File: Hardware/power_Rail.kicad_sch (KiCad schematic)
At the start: 2 parts

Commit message: fixed some subsheets
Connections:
- net +5V renamed 12VBuck/V_out_5V

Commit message: cleaned up schematic more
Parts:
- added D5: LED, LED_SMD:LED_0603_1608Metric, symbol lhrs_misc:Blue_LED
- added R28: 250, Package_TO_SOT_SMD:SOT-23, symbol Device:R
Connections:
- net GND: now also R28.2
- net Vout: now also D5.2 (A)
- new net: D5.1 (K), R28.1

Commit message: made review changes
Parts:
- added JP2, JP3, JP4, JP5: SolderJumper_2_Open, symbol Jumper:SolderJumper_2_Open
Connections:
- net 12VBuck/V_out_5V: now also JP3.2 (B)
- net GND: now also JP3.1 (A), JP4.1 (A)
- net MUX_OUT: now also JP5.1 (A)
- net Vin: now also JP2.1 (A)
- net Vout: now also JP5.2 (B)
- new net 12VBuck/V_in_12V: JP2.2 (B), JP4.2 (B)
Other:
- note added: "Galvanically Isolated"

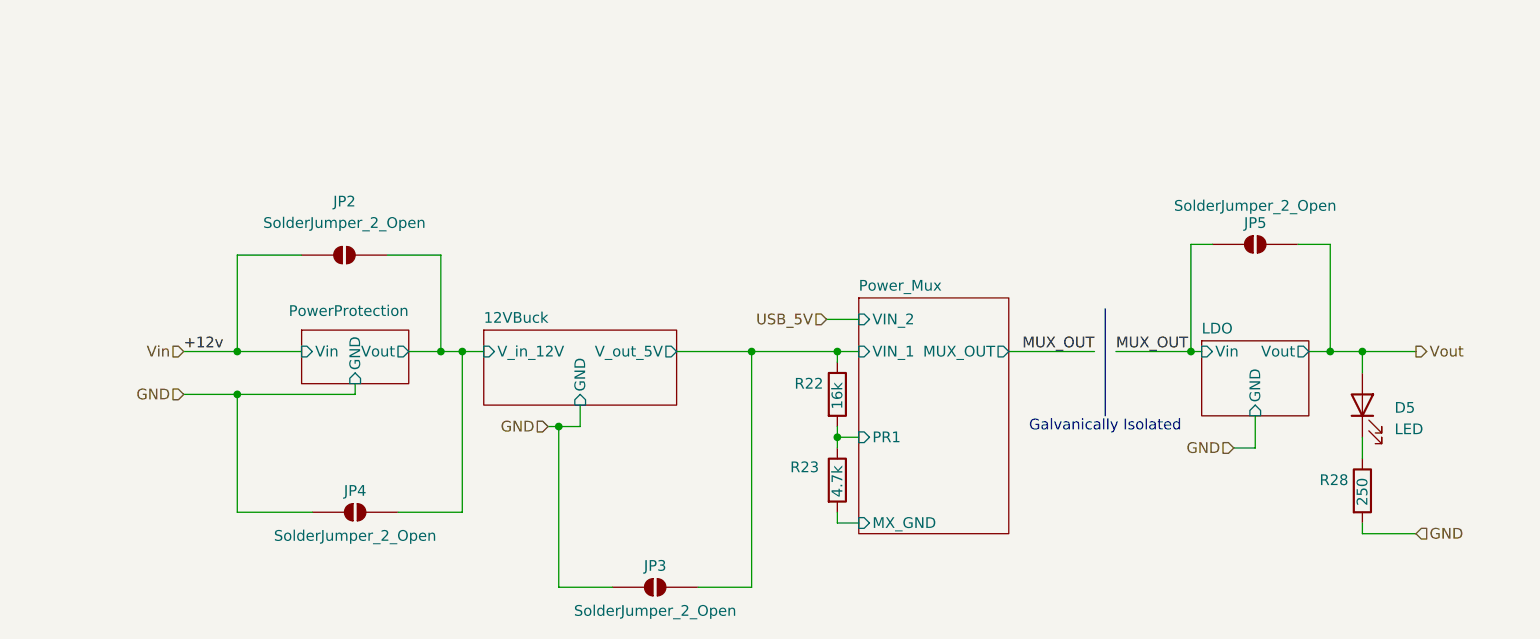
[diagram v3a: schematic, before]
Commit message: Added TestPoints
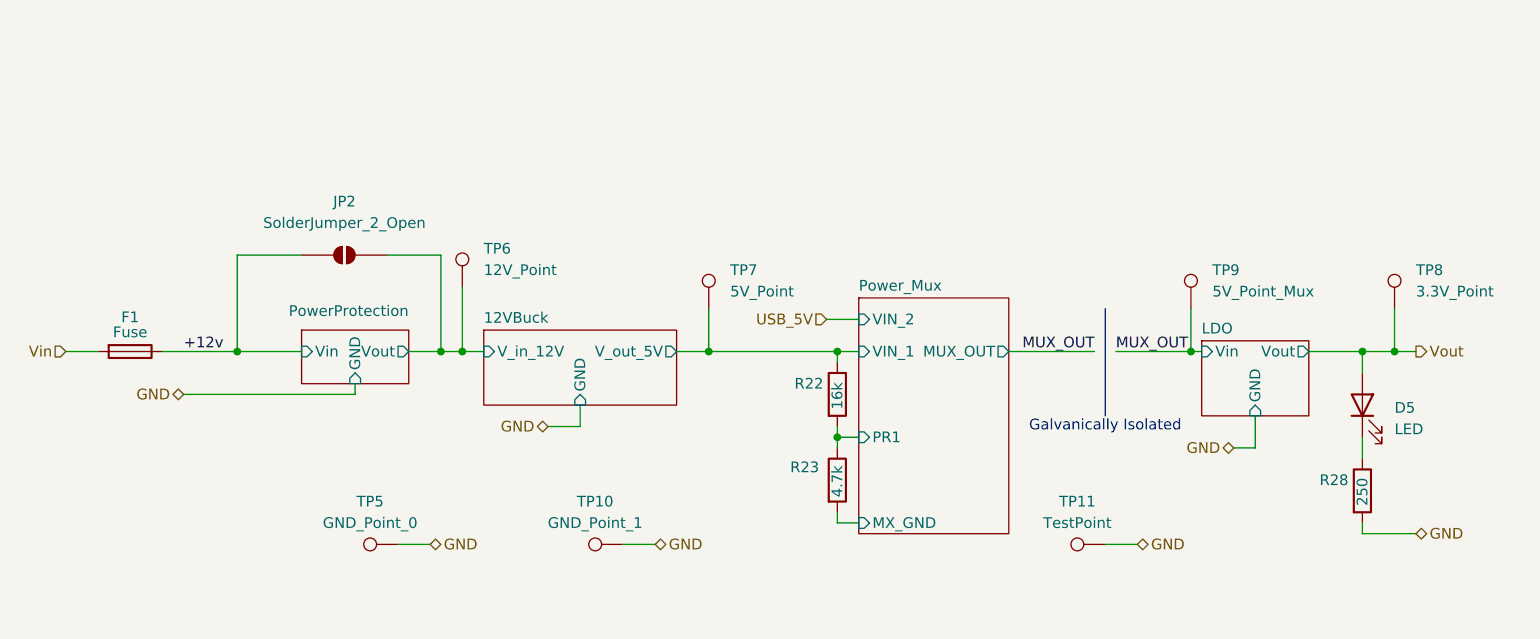
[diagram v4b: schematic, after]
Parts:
- removed JP3, JP4, JP5: SolderJumper_2_Open, symbol Jumper:SolderJumper_2_Open
- added F1: Fuse, symbol Device:Fuse
- added TP10: GND_Point_1, LHRS_Connectors:Molex_Nano-Fit_105310-xx10_2x05_P2.50mm_Vertical, symbol Connector:TestPoint
- added TP11: TestPoint, LHRS_Connectors:Molex_Nano-Fit_105310-xx10_2x05_P2.50mm_Vertical, symbol Connector:TestPoint
- added TP5: GND_Point_0, LHRS_Connectors:Molex_Nano-Fit_105310-xx10_2x05_P2.50mm_Vertical, symbol Connector:TestPoint
- added TP6: 12V_Point, LHRS_Connectors:Molex_Nano-Fit_105310-xx10_2x05_P2.50mm_Vertical, symbol Connector:TestPoint
- added TP7: 5V_Point, LHRS_Connectors:Molex_Nano-Fit_105310-xx10_2x05_P2.50mm_Vertical, symbol Connector:TestPoint
- added TP8: 3.3V_Point, LHRS_Connectors:Molex_Nano-Fit_105310-xx10_2x05_P2.50mm_Vertical, symbol Connector:TestPoint
- added TP9: 5V_Point_Mux, LHRS_Connectors:Molex_Nano-Fit_105310-xx10_2x05_P2.50mm_Vertical, symbol Connector:TestPoint
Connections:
- net 12VBuck/V_in_12V: now also TP6.1
- net 12VBuck/V_out_5V: now also TP7.1
- net GND: now also TP10.1, TP11.1, TP5.1
- net MUX_OUT: now also TP9.1
- net Vin: now also F1.2; no longer JP2.1 (A)
- net Vout: now also TP8.1
- new net +12v: F1.1, JP2.1 (A)

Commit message: Final Review Ready
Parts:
- removed D5: LED, LED_SMD:LED_0603_1608Metric, symbol lhrs_misc:Blue_LED
- removed R28: 250, Package_TO_SOT_SMD:SOT-23, symbol Device:R
- added D11, D12, D14: LED, LED_SMD:LED_0603_1608Metric_Pad1.05x0.95mm_HandSolder, symbol lhrs_misc:Blue_LED
- added R29: 1k, Package_TO_SOT_SMD:SOT-23, symbol Device:R
- added R30: 330, Package_TO_SOT_SMD:SOT-23, symbol Device:R
- added R31: 150, Package_TO_SOT_SMD:SOT-23, symbol Device:R
- added TP16: USB_5V_Point, LHRS_Connectors:Molex_Nano-Fit_105310-xx10_2x05_P2.50mm_Vertical, symbol Connector:TestPoint
- TP11: value TestPoint -> GND_Point_2
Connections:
- net +12v: now also R29.1
- net GND: now also D11.1 (K), D12.1 (K), D14.1 (K)
- net MUX_OUT: now also R30.1
- net USB_5V: now also TP16.1
- net Vout: now also R31.1
- new net: D11.2 (A), R29.2
- new net: D14.2 (A), R31.2
- new net: D12.2 (A), R30.2
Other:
- note added: "GND Test Points"
- moved on the sheet: TP10, TP11, TP5, TP6

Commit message: Final Changes before Final Review
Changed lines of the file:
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@@
 	(wire
 		(pts
-			(xy 95.25 87.63) (xy 99.06 87.63)
+			(xy 93.98 95.25) (xy 99.06 95.25)
 		)
 		(stroke
@@
 	(wire
 		(pts
-			(xy 99.06 85.09) (xy 99.06 87.63)
+			(xy 99.06 88.9) (xy 99.06 95.25)
 		)
 		(stroke
@@
 	(hierarchical_label "GND"
 		(shape bidirectional)
-		(at 95.25 87.63 180)
+		(at 93.98 95.25 180)
 		(effects
 			(font
@@
 		)
 		(instances
+			(project "power_Rail"
+				(path "/aa7870c6-fc66-461c-9d29-908d06b1b5db"
+					(reference "D11")
+					(unit 1)
+				)
+			)
 			(project "SuspensionBoard"
 				(path "/f9dc491a-b8c6-4623-9728-13837ac4bba3/bb9a0353-c4c7-4944-b892-c85c279a5c68"
@@
 		)
 		(instances
+			(project "power_Rail"
+				(path "/aa7870c6-fc66-461c-9d29-908d06b1b5db"
+					(reference "D14")
+					(unit 1)
+				)
+			)
 			(project "SuspensionBoard"
 				(path "/f9dc491a-b8c6-4623-9728-13837ac4bba3/bb9a0353-c4c7-4944-b892-c85c279a5c68"
@@
 		)
 		(instances
+			(project "power_Rail"
+				(path "/aa7870c6-fc66-461c-9d29-908d06b1b5db"
+					(reference "TP11")
+					(unit 1)
+				)
+			)
 			(project "SuspensionBoard"
 				(path "/f9dc491a-b8c6-4623-9728-13837ac4bba3/bb9a0353-c4c7-4944-b892-c85c279a5c68"
@@
 		)
 		(instances
+			(project "power_Rail"
+				(path "/aa7870c6-fc66-461c-9d29-908d06b1b5db"
+					(reference "TP5")
+					(unit 1)
+				)
+			)
 			(project "SuspensionBoard"
 				(path "/f9dc491a-b8c6-4623-9728-13837ac4bba3/bb9a0353-c4c7-4944-b892-c85c279a5c68"
@@
 		)
 		(instances
+			(project "power_Rail"
+				(path "/aa7870c6-fc66-461c-9d29-908d06b1b5db"
+					(reference "TP7")
+					(unit 1)
+				)
+			)
 			(project "SuspensionBoard"
 				(path "/f9dc491a-b8c6-4623-9728-13837ac4bba3/bb9a0353-c4c7-4944-b892-c85c279a5c68"
@@
 		)
 		(instances
+			(project "power_Rail"
+				(path "/aa7870c6-fc66-461c-9d29-908d06b1b5db"
+					(reference "R29")
+					(unit 1)
+				)
+			)
 			(project "SuspensionBoard"
 				(path "/f9dc491a-b8c6-4623-9728-13837ac4bba3/bb9a0353-c4c7-4944-b892-c85c279a5c68"
@@
 		)
 		(instances
+			(project "power_Rail"
+				(path "/aa7870c6-fc66-461c-9d29-908d06b1b5db"
+					(reference "R31")
+					(unit 1)
+				)
+			)
 			(project "SuspensionBoard"
 				(path "/f9dc491a-b8c6-4623-9728-13837ac4bba3/bb9a0353-c4c7-4944-b892-c85c279a5c68"
@@
 		)
 		(instances
+			(project "power_Rail"
+				(path "/aa7870c6-fc66-461c-9d29-908d06b1b5db"
+					(reference "TP6")
+					(unit 1)
+				)
+			)
 			(project "SuspensionBoard"
 				(path "/f9dc491a-b8c6-4623-9728-13837ac4bba3/bb9a0353-c4c7-4944-b892-c85c279a5c68"
@@
 		)
 		(instances
+			(project "power_Rail"
+				(path "/aa7870c6-fc66-461c-9d29-908d06b1b5db"
+					(reference "TP16")
+					(unit 1)
+				)
+			)
 			(project "SuspensionBoard"
 				(path "/f9dc491a-b8c6-4623-9728-13837ac4bba3/bb9a0353-c4c7-4944-b892-c85c279a5c68"
@@
 		)
 		(instances
+			(project "power_Rail"
+				(path "/aa7870c6-fc66-461c-9d29-908d06b1b5db"
+					(reference "TP8")
+					(unit 1)
+				)
+			)
 			(project "SuspensionBoard"
 				(path "/f9dc491a-b8c6-4623-9728-13837ac4bba3/bb9a0353-c4c7-4944-b892-c85c279a5c68"
@@
 		)
 		(instances
+			(project "power_Rail"
+				(path "/aa7870c6-fc66-461c-9d29-908d06b1b5db"
+					(reference "F1")
+					(unit 1)
+				)
+			)
 			(project "SuspensionBoard"
 				(path "/f9dc491a-b8c6-4623-9728-13837ac4bba3/bb9a0353-c4c7-4944-b892-c85c279a5c68"
@@
 		)
 		(instances
+			(project "power_Rail"
+				(path "/aa7870c6-fc66-461c-9d29-908d06b1b5db"
+					(reference "D12")
+					(unit 1)
+				)
+			)
 			(project "SuspensionBoard"
 				(path "/f9dc491a-b8c6-4623-9728-13837ac4bba3/bb9a0353-c4c7-4944-b892-c85c279a5c68"
@@
 		)
 		(instances
+			(project "power_Rail"
+				(path "/aa7870c6-fc66-461c-9d29-908d06b1b5db"
+					(reference "R30")
+					(unit 1)
+				)
+			)
 			(project "SuspensionBoard"
 				(path "/f9dc491a-b8c6-4623-9728-13837ac4bba3/bb9a0353-c4c7-4944-b892-c85c279a5c68"
@@
 		)
 		(instances
+			(project "power_Rail"
+				(path "/aa7870c6-fc66-461c-9d29-908d06b1b5db"
+					(reference "R23")
+					(unit 1)
+				)
+			)
 			(project "SuspensionBoard"
 				(path "/f9dc491a-b8c6-4623-9728-13837ac4bba3/bb9a0353-c4c7-4944-b892-c85c279a5c68"
@@
 		)
 		(instances
+			(project "power_Rail"
+				(path "/aa7870c6-fc66-461c-9d29-908d06b1b5db"
+					(reference "R22")
+					(unit 1)
+				)
+			)
 			(project "SuspensionBoard"
 				(path "/f9dc491a-b8c6-4623-9728-13837ac4bba3/bb9a0353-c4c7-4944-b892-c85c279a5c68"
@@
 		)
 		(instances
+			(project "power_Rail"
+				(path "/aa7870c6-fc66-461c-9d29-908d06b1b5db"
+					(reference "TP9")
+					(unit 1)
+				)
+			)
 			(project "SuspensionBoard"
 				(path "/f9dc491a-b8c6-4623-9728-13837ac4bba3/bb9a0353-c4c7-4944-b892-c85c279a5c68"
@@
 		)
 		(instances
+			(project "power_Rail"
+				(path "/aa7870c6-fc66-461c-9d29-908d06b1b5db"
+					(reference "JP2")
+					(unit 1)
+				)
+			)
 			(project "SuspensionBoard"
 				(path "/f9dc491a-b8c6-4623-9728-13837ac4bba3/bb9a0353-c4c7-4944-b892-c85c279a5c68"
@@
 		)
 		(instances
+			(project "power_Rail"
+				(path "/aa7870c6-fc66-461c-9d29-908d06b1b5db"
+					(reference "TP10")
+					(unit 1)
+				)
+			)
 			(project "SuspensionBoard"
 				(path "/f9dc491a-b8c6-4623-9728-13837ac4bba3/bb9a0353-c4c7-4944-b892-c85c279a5c68"
@@
 				)
 			)
+			(project "power_Rail"
+				(path "/aa7870c6-fc66-461c-9d29-908d06b1b5db"
+					(page "4")
+				)
+			)
 		)
 	)
@@
 				)
 			)
+			(project "power_Rail"
+				(path "/aa7870c6-fc66-461c-9d29-908d06b1b5db"
+					(page "3")
+				)
+			)
 		)
 	)
@@
 				)
 			)
+			(project "power_Rail"
+				(path "/aa7870c6-fc66-461c-9d29-908d06b1b5db"
+					(page "5")
+				)
+			)
 		)
 	)
 	(sheet
 		(at 92.71 78.74)
-		(size 12.7 6.35)
+		(size 12.7 10.16)
 		(exclude_from_sim no)
 		(in_bom yes)
@@
 		)
 		(pin "GND" input
-			(at 99.06 85.09 270)
+			(at 99.06 88.9 270)
 			(effects
 				(font
@@
 				)
 			)
-		)
-	)
+			(project "power_Rail"
+				(path "/aa7870c6-fc66-461c-9d29-908d06b1b5db"
+					(page "2")
+				)
+			)
+		)
+	)
+	(sheet_instances
+		(path "/"
+			(page "1")
+		)
+	)

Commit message: Updated KiCAD Sharepoint
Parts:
- removed TP6: 12V_Point, LHRS_Connectors:Molex_Nano-Fit_105310-xx10_2x05_P2.50mm_Vertical, symbol Connector:TestPoint
- JP2: value SolderJumper_2_Open -> PP_Bypass
- R29: value 1k -> 5k
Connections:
- net MUX_OUT renamed LDO/Vin
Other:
- note removed: "Galvanically Isolated"
- moved on the sheet: D14, R31, TP8, TP9

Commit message: Made some changes
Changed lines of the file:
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@@
+	)
+	(sheet
+		(at 198.12 77.47)
+		(size 12.7 11.43)
+		(exclude_from_sim no)
+		(in_bom yes)
+		(on_board yes)
+		(dnp no)
+		(fields_autoplaced yes)
+		(stroke
+			(width 0.1524)
+			(type solid)
+		)
+		(fill
+			(color 0 0 0 0)
+		)
+		(property "Sheetname" "LDO"
+			(at 198.12 76.7584 0)
+			(show_name no)
+			(do_not_autoplace no)
+			(effects
+				(font
+					(size 1.27 1.27)
+				)
+				(justify left bottom)
+			)
+		)
+		(property "Sheetfile" "LDO.kicad_sch"
+			(at 198.12 89.4846 0)
+			(hide yes)
+			(show_name no)
+			(do_not_autoplace no)
+			(effects
+				(font
+					(size 1.27 1.27)
+				)
+				(justify left top)
+			)
+		)
+		(pin "GND" input
+			(at 204.47 88.9 270)
+			(effects
+				(font
+					(size 1.27 1.27)
+				)
+				(justify left)
+			)
+		)
+		(pin "Vin" input
+			(at 198.12 81.28 180)
+			(effects
+				(font
+					(size 1.27 1.27)
+				)
+				(justify left)
+			)
+		)
+		(pin "Vout" output
+			(at 210.82 81.28 0)
+			(effects
+				(font
+					(size 1.27 1.27)
+				)
+				(justify right)
+			)
+		)
+		(instances
+			(project "SuspensionBoard"
+				(path "/f9dc491a-b8c6-4623-9728-13837ac4bba3/bb9a0353-c4c7-4944-b892-c85c279a5c68"
+					(page "4")
+				)
+			)
+		)
+	)
+	(sheet
+		(at 92.71 76.2)
+		(size 12.7 12.7)
+		(exclude_from_sim no)
+		(in_bom yes)
+		(on_board yes)
+		(dnp no)
+		(fields_autoplaced yes)
+		(stroke
+			(width 0.1524)
+			(type solid)
+		)
+		(fill
+			(color 0 0 0 0)
+		)
+		(property "Sheetname" "PowerProtection"
+			(at 92.71 75.4884 0)
+			(show_name no)
+			(do_not_autoplace no)
+			(effects
+				(font
+					(size 1.27 1.27)
+				)
+				(justify left bottom)
+			)
+		)
+		(property "Sheetfile" "PowerProtection.kicad_sch"
+			(at 92.71 89.4846 0)
+			(hide yes)
+			(show_name no)
+			(do_not_autoplace no)
+			(effects
+				(font
+					(size 1.27 1.27)
+				)
+				(justify left top)
+			)
+		)
+		(pin "GND" input
+			(at 99.06 88.9 270)
+			(effects
+				(font
+					(size 1.27 1.27)
+				)
+				(justify left)
+			)
+		)
+		(pin "Vin" input
+			(at 92.71 81.28 180)
+			(effects
+				(font
+					(size 1.27 1.27)
+				)
+				(justify left)
+			)
+		)
+		(pin "Vout" output
+			(at 105.41 81.28 0)
+			(effects
+				(font
+					(size 1.27 1.27)
+				)
+				(justify right)
+			)
+		)
+		(instances
+			(project "SuspensionBoard"
+				(path "/f9dc491a-b8c6-4623-9728-13837ac4bba3/bb9a0353-c4c7-4944-b892-c85c279a5c68"
+					(page "7")
+				)
+			)
+		)
+	)
+	(sheet
+		(at 114.3 77.47)
+		(size 22.86 10.16)
+		(exclude_from_sim no)
+		(in_bom yes)
+		(on_board yes)
+		(dnp no)
+		(fields_autoplaced yes)
+		(stroke
+			(width 0.1524)
+			(type solid)
+		)
+		(fill
+			(color 0 0 0 0)
+		)
+		(property "Sheetname" "12VBuck"
+			(at 114.3 76.7584 0)
+			(show_name no)
+			(do_not_autoplace no)
+			(effects
+				(font
+					(size 1.27 1.27)
+				)
+				(justify left bottom)
+			)
+		)
+		(property "Sheetfile" "12VBuck.kicad_sch"
+			(at 114.3 88.2146 0)
+			(hide yes)
+			(show_name no)
+			(do_not_autoplace no)
+			(effects
+				(font
+					(size 1.27 1.27)
+				)
+				(justify left top)
+			)
+		)
+		(pin "GND" input
+			(at 125.73 87.63 270)
+			(effects
+				(font
+					(size 1.27 1.27)
+				)
+				(justify left)
+			)
+		)
+		(pin "V_in_12V" input
+			(at 114.3 81.28 180)
+			(effects
+				(font
+					(size 1.27 1.27)
+				)
+				(justify left)
+			)
+		)
+		(pin "V_out_5V" output
+			(at 137.16 81.28 0)
+			(effects
+				(font
+					(size 1.27 1.27)
+				)
+				(justify right)
+			)
+		)
+		(instances
+			(project "SuspensionBoard"
+				(path "/f9dc491a-b8c6-4623-9728-13837ac4bba3/bb9a0353-c4c7-4944-b892-c85c279a5c68"
+					(page "3")
+				)
+			)
+		)
 	)
 	(sheet
@@
 				)
 			)
-			(project "power_Rail"
-				(path "/aa7870c6-fc66-461c-9d29-908d06b1b5db"
-					(page "4")
-				)
-			)
-		)
-	)
-	(sheet
-		(at 114.3 78.74)
-		(size 22.86 8.89)
-		(exclude_from_sim no)
-		(in_bom yes)
-		(on_board yes)
-		(dnp no)
-		(stroke
-			(width 0.1524)
-			(type solid)
-		)
-		(fill
-			(color 0 0 0 0)
-		)
-		(property "Sheetname" "12VBuck"
-			(at 114.3 78.0284 0)
-			(show_name no)
-			(do_not_autoplace no)
-			(effects
-				(font
-					(size 1.27 1.27)
-				)
-				(justify left bottom)
-			)
-		)
-		(property "Sheetfile" "12VBuck.kicad_sch"
-			(at 114.3 73.66 0)
-			(hide yes)
-			(show_name no)
-			(do_not_autoplace no)
-			(effects
-				(font
-					(size 1.27 1.27)
-				)
-				(justify left top)
-			)
-		)
-		(pin "GND" input
-			(at 125.73 87.63 270)
-			(effects
-				(font
-					(size 1.27 1.27)
-				)
-				(justify left)
-			)
-		)
-		(pin "V_in_12V" input
-			(at 114.3 81.28 180)
-			(effects
-				(font
-					(size 1.27 1.27)
-				)
-				(justify left)
-			)
-		)
-		(pin "V_out_5V" output
-			(at 137.16 81.28 0)
-			(effects
-				(font
-					(size 1.27 1.27)
-				)
-				(justify right)
-			)
-		)
-		(instances
-			(project "SuspensionBoard"
-				(path "/f9dc491a-b8c6-4623-9728-13837ac4bba3/bb9a0353-c4c7-4944-b892-c85c279a5c68"
-					(page "3")
-				)
-			)
-			(project "power_Rail"
-				(path "/aa7870c6-fc66-461c-9d29-908d06b1b5db"
-					(page "3")
-				)
-			)
-		)
-	)
-	(sheet
-		(at 198.12 80.01)
-		(size 12.7 8.89)
-		(exclude_from_sim no)
-		(in_bom yes)
-		(on_board yes)
-		(dnp no)
-		(stroke
-			(width 0.1524)
-			(type solid)
-		)
-		(fill
-			(color 0 0 0 0)
-		)
-		(property "Sheetname" "LDO"
-			(at 198.12 79.2984 0)
-			(show_name no)
-			(do_not_autoplace no)
-			(effects
-				(font
-					(size 1.27 1.27)
-				)
-				(justify left bottom)
-			)
-		)
-		(property "Sheetfile" "LDO.kicad_sch"
-			(at 198.12 75.946 0)
-			(hide yes)
-			(show_name no)
-			(do_not_autoplace no)
-			(effects
-				(font
-					(size 1.27 1.27)
-				)
-				(justify left top)
-			)
-		)
-		(pin "GND" input
-			(at 204.47 88.9 270)
-			(effects
-				(font
-					(size 1.27 1.27)
-				)
-				(justify left)
-			)
-		)
-		(pin "Vin" input
-			(at 198.12 81.28 180)
-			(effects
-				(font
-					(size 1.27 1.27)
-				)
-				(justify left)
-			)
-		)
-		(pin "Vout" output
-			(at 210.82 81.28 0)
-			(effects
-				(font
-					(size 1.27 1.27)
-				)
-				(justify right)
-			)
-		)
-		(instances
-			(project "SuspensionBoard"
-				(path "/f9dc491a-b8c6-4623-9728-13837ac4bba3/bb9a0353-c4c7-4944-b892-c85c279a5c68"
-					(page "4")
-				)
-			)
-			(project "power_Rail"
-				(path "/aa7870c6-fc66-461c-9d29-908d06b1b5db"
-					(page "5")
-				)
-			)
-		)
-	)
-	(sheet
-		(at 92.71 78.74)
-		(size 12.7 10.16)
-		(exclude_from_sim no)
-		(in_bom yes)
-		(on_board yes)
-		(dnp no)
-		(stroke
-			(width 0.1524)
-			(type solid)
-		)
-		(fill
-			(color 0 0 0 0)
-		)
-		(property "Sheetname" "PowerProtection"
-			(at 91.186 77.216 0)
-			(show_name no)
-			(do_not_autoplace no)
-			(effects
-				(font
-					(size 1.27 1.27)
-				)
-				(justify left bottom)
-			)
-		)
-		(property "Sheetfile" "PowerProtection.kicad_sch"
-			(at 86.614 73.406 0)
-			(hide yes)
-			(show_name no)
-			(do_not_autoplace no)
-			(effects
-				(font
-					(size 1.27 1.27)
-				)
-				(justify left top)
-			)
-		)
-		(pin "GND" input
-			(at 99.06 88.9 270)
-			(effects
-				(font
-					(size 1.27 1.27)
-				)
-				(justify left)
-			)
-		)
-		(pin "Vin" input
-			(at 92.71 81.28 180)
-			(effects
-				(font
-					(size 1.27 1.27)
-				)
-				(justify left)
-			)
-		)
-		(pin "Vout" output
-			(at 105.41 81.28 0)
-			(effects
-				(font
-					(size 1.27 1.27)
-				)
-				(justify right)
-			)
-		)
-		(instances
-			(project "SuspensionBoard"
-				(path "/f9dc491a-b8c6-4623-9728-13837ac4bba3/bb9a0353-c4c7-4944-b892-c85c279a5c68"
-					(page "7")
-				)
-			)
-			(project "power_Rail"
-				(path "/aa7870c6-fc66-461c-9d29-908d06b1b5db"
-					(page "2")
-				)
-			)
